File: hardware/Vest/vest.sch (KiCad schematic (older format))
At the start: 41 parts, among them P1 USB_B, P2 USB_B, Q1 BC547, Q2 BC547, Q3 BC547

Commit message: Updated pcb
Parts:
- removed Buzzer1: CONN_01X02, Pin_Headers:Pin_Header_Straight_1x02, symbol CONN_01X02
- removed Buzzer_Tran1, Q1, Q2, Q3, Vib_Tran1: BC547, TO_SOT_Packages_THT:TO-92_Inline_Wide, symbol BC547
- removed R17: R, Resistors_SMD:R_1206, symbol R
- added L1: INDUCTOR_SMALL, symbol INDUCTOR_SMALL
- added LF_DATA1, LS_CLK1: BSS138, TO_SOT_Packages_SMD:SOT-23, symbol BSS138
- added Q4, Q5: PZT2222A, TO_SOT_Packages_SMD:SOT-23, symbol PZT2222A
- added R24: 10K, Resistors_SMD:R_1206, symbol R
- added R25: 1K, Resistors_SMD:R_1206, symbol R
- added SP1: SPEAKER, Buzzers_Beepers:MagneticBuzzer_Kingstate_KCG0601, symbol SPEAKER
- R1, R10, R12, R13, R14, R15, R16: value R -> 0
- R11, R4, R6: value R0 -> 0
- R2: value R -> 10K
- R3, Re1, Re2: value R -> 1K
- R5: value R0 -> R; footprint Resistors_SMD:R_1206 -> Resistors_SMD:R_2010
- Rc2: value R -> 10
- gave numbers to parts that had none: 4
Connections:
- net A0: now also LF_DATA1.2 (S), R24.2; no longer R1.2
- net A1: now also LS_CLK1.2 (S)
- net A2: no longer R3.2
- net CE: now also NRF24L1.3 (P3)
- net CSN: now also NRF24L1.4 (P4); no longer R16.1
- net GND: now also R10.1, R10.2, R11.2, R12.2, R13.2, R14.2, R15.1, R16.1; no longer R12.1, R5.1, Re2.1, uP1.20 (GND3)
- net IRQ: now also R5.1; no longer NRF24L1.1 (P1)
- net MISO: now also NRF24L1.7 (P7); no longer R14.1
- net MOSI: now also NRF24L1.6 (P6); no longer NRF24L1.3 (P3)
- net PIN10_OUT: now also Re2.1
- net PIN6: now also Re1.2
- net RAW: now also LEDs1.1 (P1), R3.1, R25.1
- net SCK: now also NRF24L1.5 (P5); no longer NRF24L1.4 (P4)
- net VCC: now also R1.1, R1.2, R2.1, R6.1, R6.2, R9.1, L1.1, LF_DATA1.1 (G), LS_CLK1.1 (G), R24.1, SP1.1; no longer LEDs1.1 (P1), NRF24L1.7 (P7), P1.1 (VCC)
- net VCC_J: now also P1.1 (VCC)
- net at Rc2.1: now also Q5.2 (C)
- net at Re2.2: now also Q5.1 (B)
- net at Rc1.1: now also Q4.2 (C)
- net at Re1.1: now also Q4.1 (B)
- net at Rc2.2: now also L1.2, SP1.2
- net LED_DATA: now reaches LEDs1.2 (P2)
- net LED_DATA: now also LF_DATA1.3 (D), R25.2
- net LED_CLK: now reaches LEDs1.3 (P3)
- net LED_CLK: now also R3.2, LS_CLK1.3 (D)
- net at LEDs1.4 (P4): now also R11.1
- net at R4.1: now also Mic1.3 (P3); no longer R11.2
- net at R7.1: now also NRF24L1.1 (P1); no longer R14.2
- net at R16.2: now also Q5.3 (E); no longer R13.1
- net CE_OUT: no longer names the net of R15.2
- net CE_OUT: now also Q4.3 (E); no longer NRF24L1.6 (P6)
- net CSN_OUT: no longer names the net of R9.2
- net CSN_OUT: now also NRF24L1.2 (P2); no longer NRF24L1.5 (P5)
- removed net GND_J: Belt1.4 (P4), IR1.3 (P3), Mic1.3 (P3), R11.1, Re1.2
- net GND_J2: no longer names the net of R5.2
- net GND_J2: now also NRF24L1.8 (P8); no longer R6.2
- removed net GND_OUT: NRF24L1.8 (P8), R10.2
- net MISO_OUT: no longer names the net of R7.2
- net MISO_OUT: now also R13.1; no longer NRF24L1.2 (P2)
- net RX renamed RX_to_weapon_TX
- net TX renamed TX_to_weapon_RX
- new net: IR1.3 (P3), R12.1
- new net: Belt1.4 (P4), R14.1
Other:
- moved on the sheet: IR1, Mic1, Re1, Re2

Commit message: Added 2 more connectors
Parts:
- removed Q4, Q5: PZT2222A, TO_SOT_Packages_SMD:SOT-23, symbol PZT2222A
- added LEDs2, LEDs3: CONN_01X04, Pin_Headers:Pin_Header_Straight_1x04, symbol CONN_01X04
- added Q1, Q2: MMBT3904, TO_SOT_Packages_SMD:SOT-23, symbol MMBT3904
- added R17, R23, R26, R27: 0, Resistors_SMD:R_1206, symbol R
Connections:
- net GND: now also LEDs3.4 (P4), R26.2
- net RAW: now also R17.2, R23.2, R27.2; no longer LEDs1.1 (P1)
- net at Rc2.1: now also Q2.3 (C)
- net at Re2.2: now also Q2.1 (B)
- net at Rc1.1: now also Q1.3 (C)
- net at Re1.1: now also Q1.1 (B)
- net at R16.2: now also Q2.2 (E)
- net at R15.2: now also Q1.2 (E)
- new net: LEDs1.1 (P1), R17.1
- new net: LEDs2.1 (P1), R23.1
- new net: LEDs2.4 (P4), R26.1
- new net: LEDs3.1 (P1), R27.1
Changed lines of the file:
@@
 Text GLabel 3500 4300 0    60   Input ~ 0
 PIN4
-Text GLabel 6050 6200 0    60   Input ~ 0
+Text GLabel 5750 6200 0    60   Input ~ 0
 RAW
 Text GLabel 4700 4200 2    60   Input ~ 0
@@
 VCC_J
 $Comp
-L PZT2222A Q5
-U 1 1 584F0E2C
-P 6600 2550
-F 0 "Q5" H 6800 2625 50  0000 L CNN
-F 1 "PZT2222A" H 6800 2550 50  0000 L CNN
-F 2 "TO_SOT_Packages_SMD:SOT-23" H 6800 2475 50  0000 L CIN
-F 3 "" H 6600 2550 50  0000 L CNN
-	1    6600 2550
-	1    0    0    -1
-$EndComp
-$Comp
 L SPEAKER SP1
 U 1 1 584F19DF
@@
 	1    6700 1500
 	0    1    1    0
-$EndComp
-$Comp
-L PZT2222A Q4
-U 1 1 584F2792
-P 1600 3200
-F 0 "Q4" H 1800 3275 50  0000 L CNN
-F 1 "PZT2222A" H 1800 3200 50  0000 L CNN
-F 2 "TO_SOT_Packages_SMD:SOT-23" H 1800 3125 50  0000 L CIN
-F 3 "" H 1600 3200 50  0000 L CNN
-	1    1600 3200
-	1    0    0    -1
 $EndComp
 $Comp
@@
 	-1   0    0    1
 $EndComp
+$Comp
+L MMBT3904 Q1
+U 1 1 584FEB5A
+P 1600 3200
+F 0 "Q1" H 1800 3275 50  0000 L CNN
+F 1 "MMBT3904" H 1800 3200 50  0000 L CNN
+F 2 "TO_SOT_Packages_SMD:SOT-23" H 1800 3125 50  0000 L CIN
+F 3 "" H 1600 3200 50  0000 L CNN
+	1    1600 3200
+	1    0    0    -1
+$EndComp
+$Comp
+L MMBT3904 Q2
+U 1 1 584FED8D
+P 6600 2550
+F 0 "Q2" H 6800 2625 50  0000 L CNN
+F 1 "MMBT3904" H 6800 2550 50  0000 L CNN
+F 2 "TO_SOT_Packages_SMD:SOT-23" H 6800 2475 50  0000 L CIN
+F 3 "" H 6600 2550 50  0000 L CNN
+	1    6600 2550
+	1    0    0    -1
+$EndComp
+$Comp
+L R R17
+U 1 1 58506815
+P 5900 6200
+F 0 "R17" V 5980 6200 50  0000 C CNN
+F 1 "0" V 5900 6200 50  0000 C CNN
+F 2 "Resistors_SMD:R_1206" V 5830 6200 50  0001 C CNN
+F 3 "" H 5900 6200 50  0000 C CNN
+	1    5900 6200
+	0    1    1    0
+$EndComp
+$Comp
+L CONN_01X04 LEDs2
+U 1 1 58506A8E
+P 7800 5750
+F 0 "LEDs2" H 7800 6000 50  0000 C CNN
+F 1 "CONN_01X04" V 7900 5750 50  0000 C CNN
+F 2 "Pin_Headers:Pin_Header_Straight_1x04" H 7800 5750 50  0001 C CNN
+F 3 "" H 7800 5750 50  0000 C CNN
+	1    7800 5750
+	1    0    0    -1
+$EndComp
+Text GLabel 7200 5600 0    60   Input ~ 0
+RAW
+Text GLabel 7300 5900 0    60   Input ~ 0
+GND
+$Comp
+L CONN_01X04 LEDs3
+U 1 1 58506C53
+P 8850 5550
+F 0 "LEDs3" H 8850 5800 50  0000 C CNN
+F 1 "CONN_01X04" V 8950 5550 50  0000 C CNN
+F 2 "Pin_Headers:Pin_Header_Straight_1x04" H 8850 5550 50  0001 C CNN
+F 3 "" H 8850 5550 50  0000 C CNN
+	1    8850 5550
+	1    0    0    -1
+$EndComp
+Text GLabel 8350 5400 0    60   Input ~ 0
+RAW
+Text GLabel 8650 5700 0    60   Input ~ 0
+GND
+$Comp
+L R R27
+U 1 1 58507128
+P 8500 5400
+F 0 "R27" V 8580 5400 50  0000 C CNN
+F 1 "0" V 8500 5400 50  0000 C CNN
+F 2 "Resistors_SMD:R_1206" V 8430 5400 50  0001 C CNN
+F 3 "" H 8500 5400 50  0000 C CNN
+	1    8500 5400
+	0    1    1    0
+$EndComp
+$Comp
+L R R23
+U 1 1 585077AE
+P 7450 5600
+F 0 "R23" V 7530 5600 50  0000 C CNN
+F 1 "0" V 7450 5600 50  0000 C CNN
+F 2 "Resistors_SMD:R_1206" V 7380 5600 50  0001 C CNN
+F 3 "" H 7450 5600 50  0000 C CNN
+	1    7450 5600
+	0    1    1    0
+$EndComp
+Wire Wire Line
+	7200 5600 7300 5600
+$Comp
+L R R26
+U 1 1 58507960
+P 7450 5900
+F 0 "R26" V 7530 5900 50  0000 C CNN
+F 1 "0" V 7450 5900 50  0000 C CNN
+F 2 "Resistors_SMD:R_1206" V 7380 5900 50  0001 C CNN
+F 3 "" H 7450 5900 50  0000 C CNN
+	1    7450 5900
+	0    1    1    0
+$EndComp
 $EndSCHEMATC

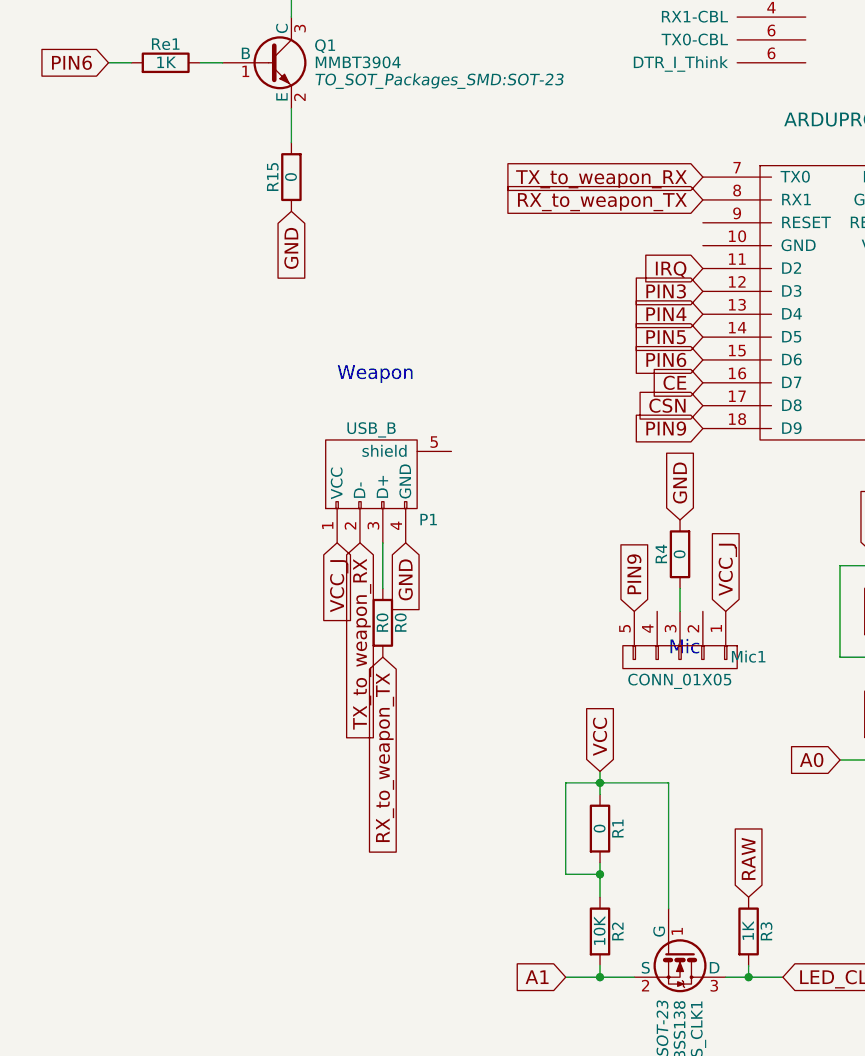
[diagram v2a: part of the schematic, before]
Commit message: minor changes to the vest schematic
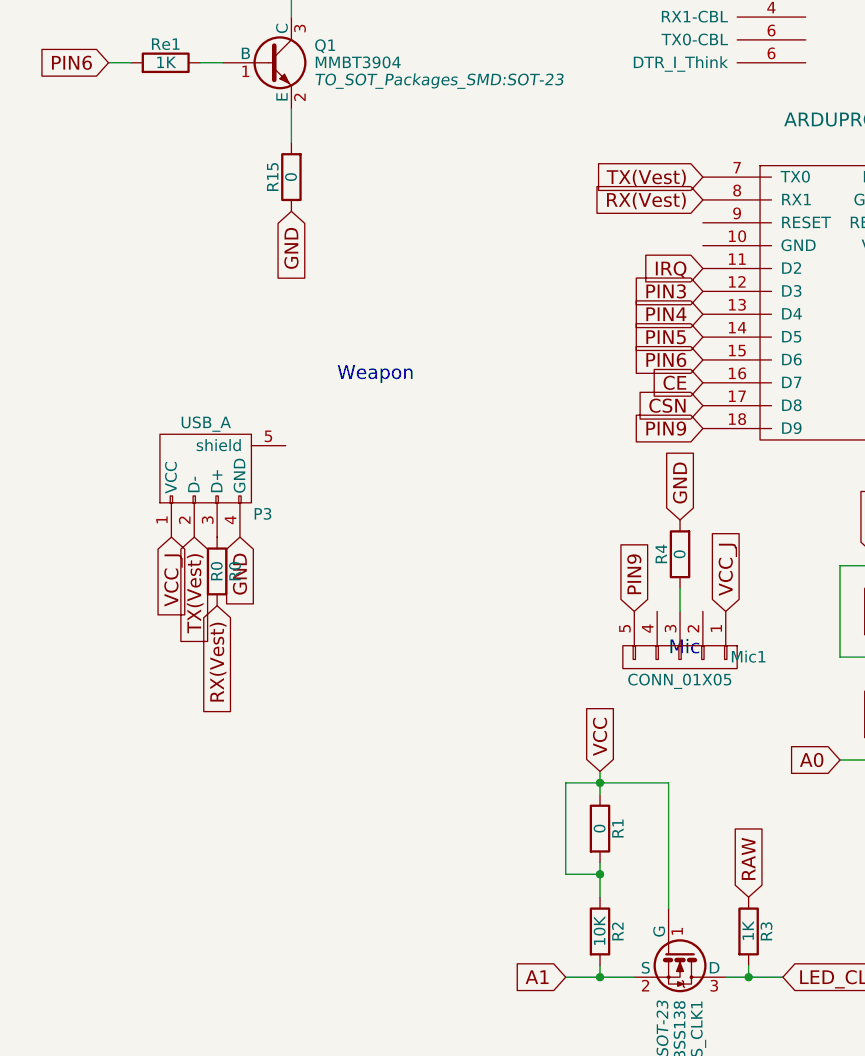
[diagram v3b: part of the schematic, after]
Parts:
- removed P1: USB_B, Connect:USB_A, symbol USB_B
- added P3: USB_A, Connect:USB_A, symbol USB_A
- L1: footprint (none) -> Resistors_SMD:R_1206
- P2: footprint Connect:USB_A -> Connect:USB_B
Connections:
- net GND: now also P3.4 (GND)
- net VCC_J: now also P3.1 (VCC)
- net at R0.1: now also P3.3 (D+)
- net RX_to_weapon_TX renamed RX(Vest)
- net TX_to_weapon_RX renamed TX(Vest)
- net TX(Vest): now also P3.2 (D-)
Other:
- moved on the sheet: R0
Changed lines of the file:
@@
 LIBS:contrib
 LIBS:valves
-LIBS:ArduProMiniTKB
 LIBS:vest-cache
 EELAYER 25 0
@@
 F 0 "P2" H 4500 1850 50  0000 C CNN
 F 1 "USB_B" H 4250 2250 50  0000 C CNN
-F 2 "Connect:USB_A" V 4250 1950 50  0001 C CNN
+F 2 "Connect:USB_B" V 4250 1950 50  0001 C CNN
 F 3 "" V 4250 1950 50  0000 C CNN
 	1    4300 2050
-	1    0    0    -1
-$EndComp
-$Comp
-L USB_B P1
-U 1 1 584CEDB8
-P 2100 5000
-F 0 "P1" H 2300 4800 50  0000 C CNN
-F 1 "USB_B" H 2050 5200 50  0000 C CNN
-F 2 "Connect:USB_A" V 2050 4900 50  0001 C CNN
-F 3 "" V 2050 4900 50  0000 C CNN
-	1    2100 5000
 	1    0    0    -1
 $EndComp
@@
 Text Notes 1900 4600 0    60   ~ 0
 Weapon\n
-Text GLabel 1900 5300 3    60   Input ~ 0
+Text GLabel 1175 5275 3    60   Input ~ 0
 VCC_J
-Text GLabel 2200 5300 3    60   Input ~ 0
-GND
-Text GLabel 2000 5300 3    60   Input ~ 0
-TX_to_weapon_RX
-Text GLabel 2100 5800 3    60   Input ~ 0
-RX_to_weapon_TX
+Text GLabel 1475 5275 3    60   Input ~ 0
+GND
 Text GLabel 3500 3700 0    60   Input ~ 0
-TX_to_weapon_RX
+TX(Vest)
 Text GLabel 3500 3800 0    60   Input ~ 0
-RX_to_weapon_TX
+RX(Vest)
 Text GLabel 3500 4100 0    60   Input ~ 0
 IRQ
@@
 L R R0
 U 1 1 584E4E76
-P 2100 5650
-F 0 "R0" V 2180 5650 50  0000 C CNN
-F 1 "R0" V 2100 5650 50  0000 C CNN
-F 2 "Resistors_SMD:R_1206" V 2030 5650 50  0001 C CNN
-F 3 "" H 2100 5650 50  0000 C CNN
-	1    2100 5650
+P 1375 5425
+F 0 "R0" V 1455 5425 50  0000 C CNN
+F 1 "R0" V 1375 5425 50  0000 C CNN
+F 2 "Resistors_SMD:R_1206" V 1305 5425 50  0001 C CNN
+F 3 "" H 1375 5425 50  0000 C CNN
+	1    1375 5425
 	1    0    0    -1
 $EndComp
@@
 F 0 "L1" H 6700 1600 50  0000 C CNN
 F 1 "INDUCTOR_SMALL" H 6700 1450 50  0000 C CNN
-F 2 "" H 6700 1500 50  0001 C CNN
+F 2 "Resistors_SMD:R_1206" H 6700 1500 50  0001 C CNN
 F 3 "" H 6700 1500 50  0000 C CNN
 	1    6700 1500
@@
 	1450 2600 1700 2600
 Wire Wire Line
-	2100 5300 2100 5500
-Wire Wire Line
 	5950 2550 6050 2550
 Wire Wire Line
@@
 	0    1    1    0
 $EndComp
+$Comp
+L USB_A P3
+U 1 1 5850C2DD
+P 1375 4975
+F 0 "P3" H 1575 4775 50  0000 C CNN
+F 1 "USB_A" H 1325 5175 50  0000 C CNN
+F 2 "Connect:USB_A" V 1325 4875 50  0001 C CNN
+F 3 "" V 1325 4875 50  0000 C CNN
+	1    1375 4975
+	1    0    0    -1
+$EndComp
+Text GLabel 1275 5275 3    60   Input ~ 0
+TX(Vest)
+Text GLabel 1375 5575 3    60   Input ~ 0
+RX(Vest)
 $EndSCHEMATC

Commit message: Updated pcb
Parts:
- P2: value USB_B -> USB_B_Power
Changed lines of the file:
@@
 P 4300 2050
 F 0 "P2" H 4500 1850 50  0000 C CNN
-F 1 "USB_B" H 4250 2250 50  0000 C CNN
+F 1 "USB_B_Power" H 4250 2250 50  0000 C CNN
 F 2 "Connect:USB_B" V 4250 1950 50  0001 C CNN
 F 3 "" V 4250 1950 50  0000 C CNN
